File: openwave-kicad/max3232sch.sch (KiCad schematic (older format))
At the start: 1 part

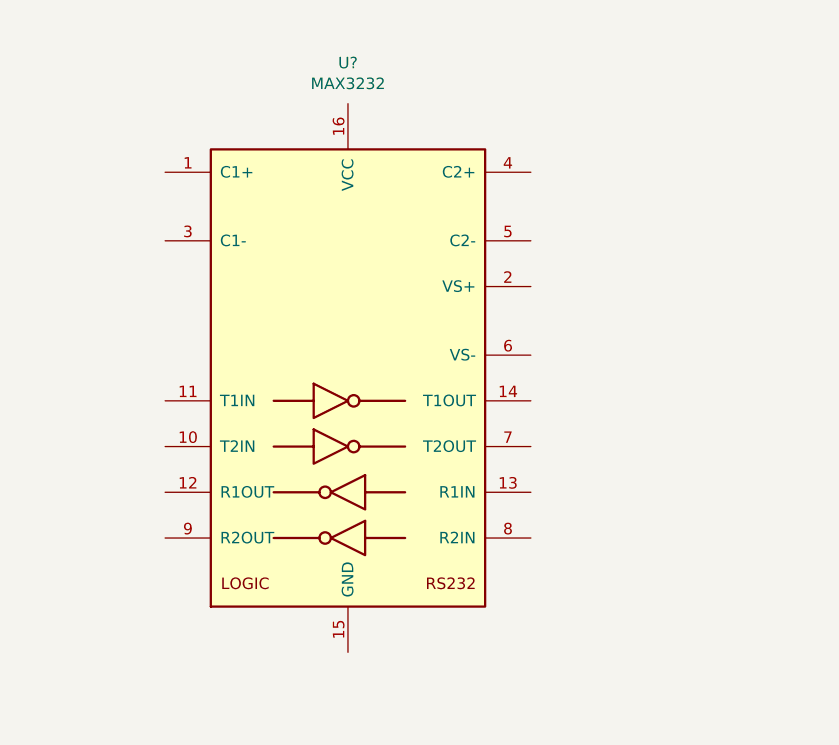
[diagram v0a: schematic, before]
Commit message: finished max232 schematic
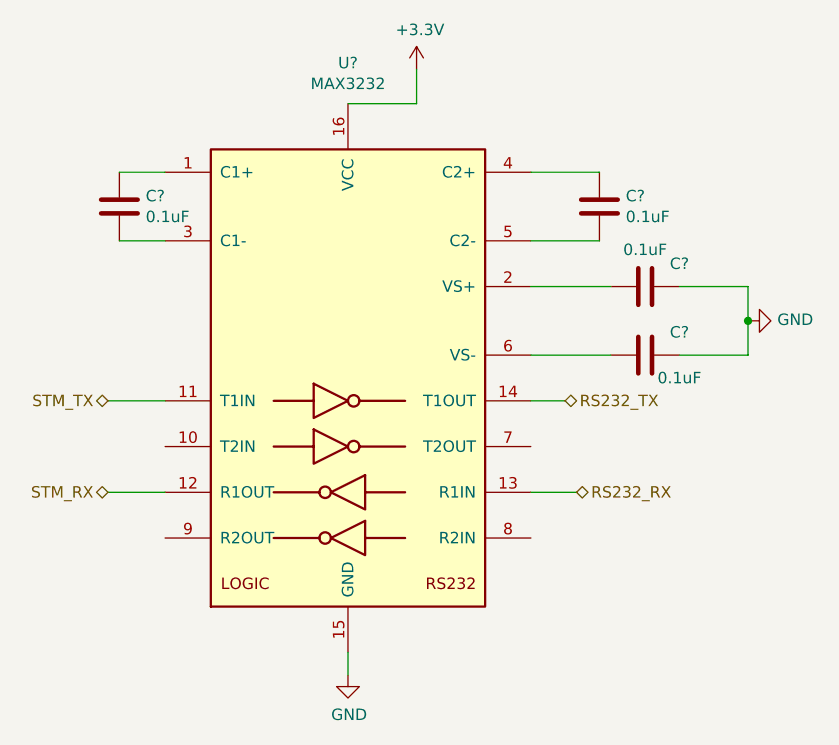
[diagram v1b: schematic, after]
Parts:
- added C? (x4): 0.1uF, symbol Device:C
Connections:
- net at U?.1 (C1+): now also C?.1
- net STM_TX: now reaches U?.11 (T1IN)
- net STM_RX: now reaches U?.12 (R1OUT)
- net RS232_RX: now reaches U?.13 (R1IN)
- net RS232_TX: now reaches U?.14 (T1OUT)
- net GND: now reaches U?.15 (GND)
- net GND: now also C?.1, C?.1
- net +3V3: now reaches U?.16 (VCC)
- net at U?.2 (VS+): now also C?.2
- net at U?.3 (C1-): now also C?.2
- net at U?.4 (C2+): now also C?.1
- net at U?.5 (C2-): now also C?.2
- net at U?.6 (VS-): now also C?.2
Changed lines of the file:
@@
 	1    0    0    -1
 $EndComp
+Wire Wire Line
+	6000 2250 6300 2250
+Wire Wire Line
+	6300 2250 6300 2100
+$Comp
+L power:+3.3V #PWR?
+U 1 1 5CC3B6BA
+P 6300 2100
+F 0 "#PWR?" H 6300 1950 50  0001 C CNN
+F 1 "+3.3V" H 6315 2273 50  0000 C CNN
+F 2 "" H 6300 2100 50  0001 C CNN
+F 3 "" H 6300 2100 50  0001 C CNN
+	1    6300 2100
+	1    0    0    -1
+$EndComp
+$Comp
+L power:GND #PWR?
+U 1 1 5CC3B721
+P 6000 4750
+F 0 "#PWR?" H 6000 4500 50  0001 C CNN
+F 1 "GND" H 6005 4577 50  0000 C CNN
+F 2 "" H 6000 4750 50  0001 C CNN
+F 3 "" H 6000 4750 50  0001 C CNN
+	1    6000 4750
+	1    0    0    -1
+$EndComp
+Wire Wire Line
+	6000 4650 6000 4750
+Wire Wire Line
+	4950 3950 5200 3950
+Text HLabel 4950 3950 0    50   BiDi ~ 0
+STM_RX
+Text HLabel 4950 3550 0    50   BiDi ~ 0
+STM_TX
+Wire Wire Line
+	4950 3550 5200 3550
+$Comp
+L Device:C C?
+U 1 1 5CC7D0DB
+P 7100 2700
+F 0 "C?" H 7215 2746 50  0000 L CNN
+F 1 "0.1uF" H 7215 2655 50  0000 L CNN
+F 2 "" H 7138 2550 50  0001 C CNN
+F 3 "~" H 7100 2700 50  0001 C CNN
+	1    7100 2700
+	1    0    0    -1
+$EndComp
+$Comp
+L Device:C C?
+U 1 1 5CC7D272
+P 5000 2700
+F 0 "C?" H 5115 2746 50  0000 L CNN
+F 1 "0.1uF" H 5115 2655 50  0000 L CNN
+F 2 "" H 5038 2550 50  0001 C CNN
+F 3 "~" H 5000 2700 50  0001 C CNN
+	1    5000 2700
+	1    0    0    -1
+$EndComp
+$Comp
+L Device:C C?
+U 1 1 5CC7D2F0
+P 7300 3050
+F 0 "C?" V 7200 3200 50  0000 C CNN
+F 1 "0.1uF" V 7139 3050 50  0000 C CNN
+F 2 "" H 7338 2900 50  0001 C CNN
+F 3 "~" H 7300 3050 50  0001 C CNN
+	1    7300 3050
+	0    1    1    0
+$EndComp
+$Comp
+L Device:C C?
+U 1 1 5CC7D32E
+P 7300 3350
+F 0 "C?" V 7200 3500 50  0000 C CNN
+F 1 "0.1uF" V 7400 3500 50  0000 C CNN
+F 2 "" H 7338 3200 50  0001 C CNN
+F 3 "~" H 7300 3350 50  0001 C CNN
+	1    7300 3350
+	0    1    1    0
+$EndComp
+Wire Wire Line
+	6800 3050 7150 3050
+Wire Wire Line
+	6800 3350 7150 3350
+$Comp
+L power:GND #PWR?
+U 1 1 5CC7D58A
+P 7750 3200
+F 0 "#PWR?" H 7750 2950 50  0001 C CNN
+F 1 "GND" V 7755 3072 50  0000 R CNN
+F 2 "" H 7750 3200 50  0001 C CNN
+F 3 "" H 7750 3200 50  0001 C CNN
+	1    7750 3200
+	0    -1   -1   0
+$EndComp
+Wire Wire Line
+	7450 3050 7750 3050
+Wire Wire Line
+	7750 3050 7750 3200
+Wire Wire Line
+	7750 3200 7750 3350
+Wire Wire Line
+	7750 3350 7450 3350
+Connection ~ 7750 3200
+Text HLabel 6950 3550 2    50   BiDi ~ 0
+RS232_TX
+Wire Wire Line
+	6800 3550 6950 3550
+Text HLabel 7000 3950 2    50   BiDi ~ 0
+RS232_RX
+Wire Wire Line
+	6800 3950 7000 3950
+Wire Wire Line
+	6800 2550 7100 2550
+Wire Wire Line
+	6800 2850 7100 2850
+Wire Wire Line
+	5200 2550 5000 2550
+Wire Wire Line
+	5200 2850 5000 2850
 $EndSCHEMATC

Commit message: linked all footprints to symbols, ready for routing
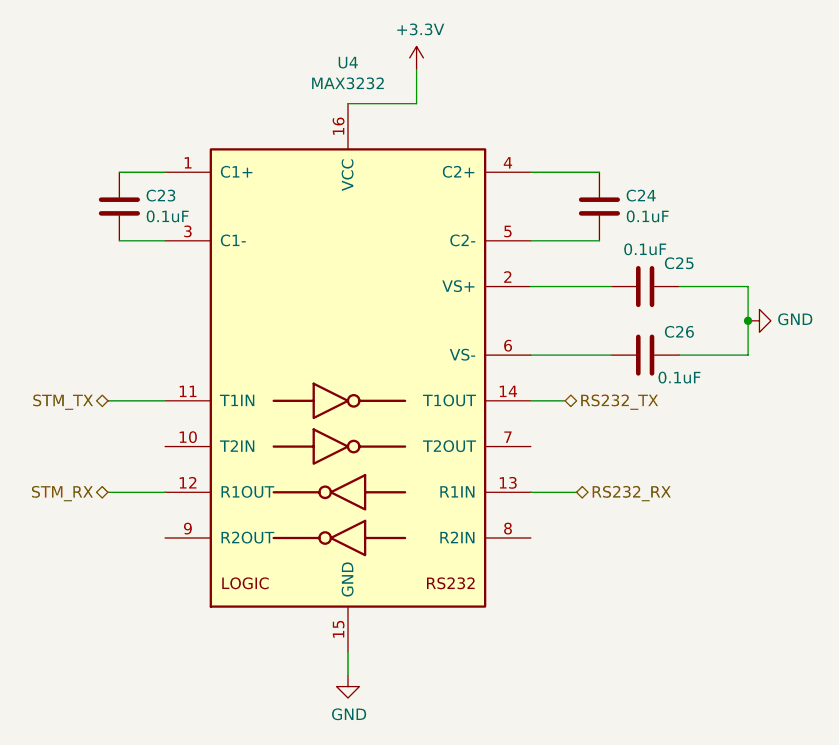
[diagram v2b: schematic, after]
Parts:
- C23, C24, C25, C26: renamed from C?; footprint (none) -> Capacitor_SMD:C_0603_1608Metric
- U4: renamed from U?; footprint (none) -> Package_SO:SOIC-16_3.9x9.9mm_P1.27mm
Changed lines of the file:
@@
 $EndDescr
 $Comp
-L Interface_UART:MAX3232 U?
+L Interface_UART:MAX3232 U4
 U 1 1 5CB14886
 P 6000 3450
-F 0 "U?" H 6000 4828 50  0000 C CNN
+F 0 "U4" H 6000 4828 50  0000 C CNN
 F 1 "MAX3232" H 6000 4737 50  0000 C CNN
-F 2 "" H 6050 2400 50  0001 L CNN
+F 2 "Package_SO:SOIC-16_3.9x9.9mm_P1.27mm" H 6050 2400 50  0001 L CNN
 F 3 "https://datasheets.maximintegrated.com/en/ds/MAX3222-MAX3241.pdf" H 6000 3550 50  0001 C CNN
 	1    6000 3450
@@
 	6300 2250 6300 2100
 $Comp
-L power:+3.3V #PWR?
+L power:+3.3V #PWR0121
 U 1 1 5CC3B6BA
 P 6300 2100
-F 0 "#PWR?" H 6300 1950 50  0001 C CNN
+F 0 "#PWR0121" H 6300 1950 50  0001 C CNN
 F 1 "+3.3V" H 6315 2273 50  0000 C CNN
 F 2 "" H 6300 2100 50  0001 C CNN
@@
 $EndComp
 $Comp
-L power:GND #PWR?
+L power:GND #PWR0122
 U 1 1 5CC3B721
 P 6000 4750
-F 0 "#PWR?" H 6000 4500 50  0001 C CNN
+F 0 "#PWR0122" H 6000 4500 50  0001 C CNN
 F 1 "GND" H 6005 4577 50  0000 C CNN
 F 2 "" H 6000 4750 50  0001 C CNN
@@
 	4950 3550 5200 3550
 $Comp
-L Device:C C?
+L Device:C C24
 U 1 1 5CC7D0DB
 P 7100 2700
-F 0 "C?" H 7215 2746 50  0000 L CNN
+F 0 "C24" H 7215 2746 50  0000 L CNN
 F 1 "0.1uF" H 7215 2655 50  0000 L CNN
-F 2 "" H 7138 2550 50  0001 C CNN
+F 2 "Capacitor_SMD:C_0603_1608Metric" H 7138 2550 50  0001 C CNN
 F 3 "~" H 7100 2700 50  0001 C CNN
 	1    7100 2700
@@
 $EndComp
 $Comp
-L Device:C C?
+L Device:C C23
 U 1 1 5CC7D272
 P 5000 2700
-F 0 "C?" H 5115 2746 50  0000 L CNN
+F 0 "C23" H 5115 2746 50  0000 L CNN
 F 1 "0.1uF" H 5115 2655 50  0000 L CNN
-F 2 "" H 5038 2550 50  0001 C CNN
+F 2 "Capacitor_SMD:C_0603_1608Metric" H 5038 2550 50  0001 C CNN
 F 3 "~" H 5000 2700 50  0001 C CNN
 	1    5000 2700
@@
 $EndComp
 $Comp
-L Device:C C?
+L Device:C C25
 U 1 1 5CC7D2F0
 P 7300 3050
-F 0 "C?" V 7200 3200 50  0000 C CNN
+F 0 "C25" V 7200 3200 50  0000 C CNN
 F 1 "0.1uF" V 7139 3050 50  0000 C CNN
-F 2 "" H 7338 2900 50  0001 C CNN
+F 2 "Capacitor_SMD:C_0603_1608Metric" H 7338 2900 50  0001 C CNN
 F 3 "~" H 7300 3050 50  0001 C CNN
 	1    7300 3050
@@
 $EndComp
 $Comp
-L Device:C C?
+L Device:C C26
 U 1 1 5CC7D32E
 P 7300 3350
-F 0 "C?" V 7200 3500 50  0000 C CNN
+F 0 "C26" V 7200 3500 50  0000 C CNN
 F 1 "0.1uF" V 7400 3500 50  0000 C CNN
-F 2 "" H 7338 3200 50  0001 C CNN
+F 2 "Capacitor_SMD:C_0603_1608Metric" H 7338 3200 50  0001 C CNN
 F 3 "~" H 7300 3350 50  0001 C CNN
 	1    7300 3350
@@
 	6800 3350 7150 3350
 $Comp
-L power:GND #PWR?
+L power:GND #PWR0123
 U 1 1 5CC7D58A
 P 7750 3200
-F 0 "#PWR?" H 7750 2950 50  0001 C CNN
+F 0 "#PWR0123" H 7750 2950 50  0001 C CNN
 F 1 "GND" V 7755 3072 50  0000 R CNN
 F 2 "" H 7750 3200 50  0001 C CNN
